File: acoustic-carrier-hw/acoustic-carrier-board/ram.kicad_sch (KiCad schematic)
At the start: 9 parts, among them IC1 ECP5-BGA256, U5 MT41K64M16TW-107_J-TR

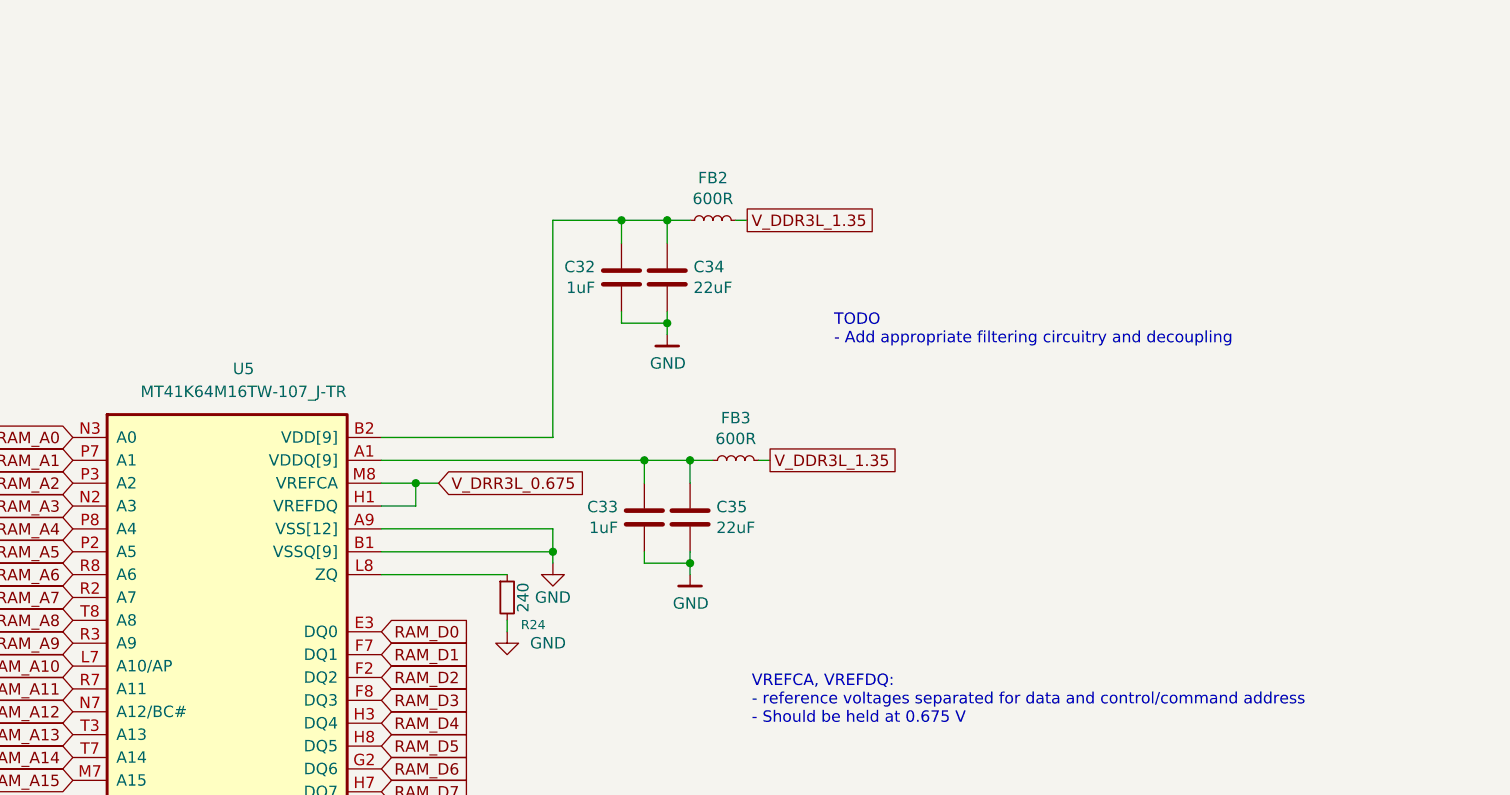
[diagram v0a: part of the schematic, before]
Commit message: [carrier] Added decoupling for DDR (next) Finish power supply
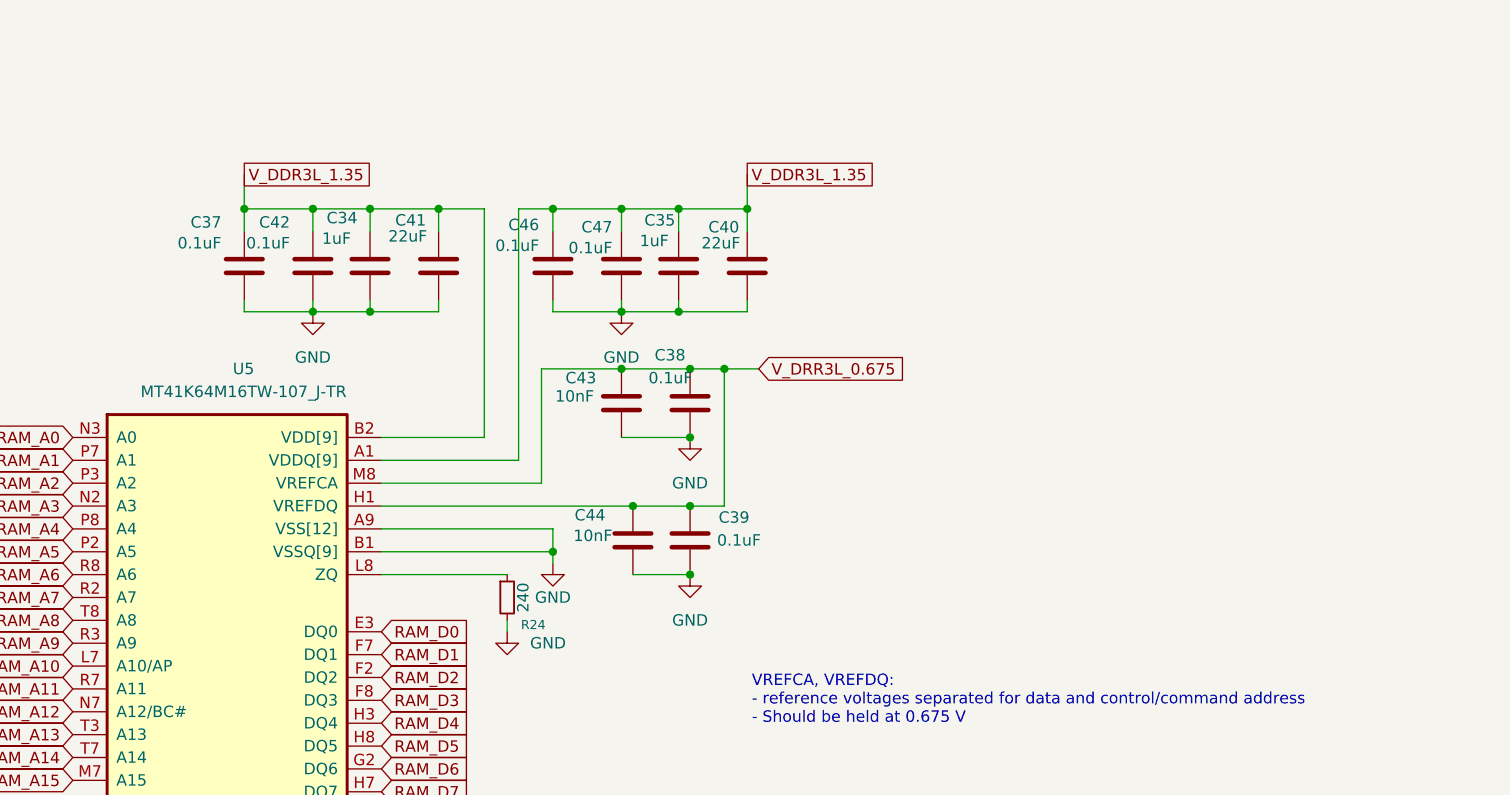
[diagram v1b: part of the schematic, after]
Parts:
- removed C32, C33: 1uF, Capacitor_SMD:C_0402_1005Metric, symbol Device:C
- removed FB2, FB3: 600R, Inductor_SMD:L_0402_1005Metric, symbol Device:L_Small
- added C37, C38, C39, C42, C46, C47: 0.1uF, Capacitor_SMD:C_0402_1005Metric, symbol Device:C
- added C40, C41: 22uF, Capacitor_SMD:C_0603_1608Metric, symbol Device:C
- added C43, C44: 10nF, Capacitor_SMD:C_0402_1005Metric, symbol Device:C
- C34, C35: value 22uF -> 1uF; footprint Capacitor_SMD:C_0603_1608Metric -> Capacitor_SMD:C_0805_2012Metric; LCSC Part Number (none) -> C28323; Manufacturing Part Number (none) -> CL21B105KBFNNNE; Mfg Murata Electronics North America -> (none); PN GRM188R60J226MEA0D -> (none)
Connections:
- net GND: now also C37.2, C38.2, C39.2, C40.2, C41.2, C42.2, C43.2, C44.2, C46.2, C47.2
- net V_DDR3L_1.35: now also C34.1, C35.1, U5.A1 (VDDQ[9]), U5.A8 (VDDQ), U5.B2 (VDD[9]), U5.C1 (VDDQ), U5.C9 (VDDQ), U5.D2 (VDDQ), U5.D9 (VDD), U5.E9 (VDDQ), U5.F1 (VDDQ), U5.G7 (VDD), U5.H2 (VDDQ), U5.H9 (VDDQ), U5.K2 (VDD), U5.K8 (VDD), U5.N1 (VDD), U5.N9 (VDD), U5.R1 (VDD), U5.R9 (VDD), C37.1, C40.1, C41.1, C42.1, C46.1, C47.1
- net V_DRR3L_0.675: now also C38.1, C39.1, C43.1, C44.1
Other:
- note removed: "TODO - Add appropriate filtering circuitry and decoupling"
- moved on the sheet: C34

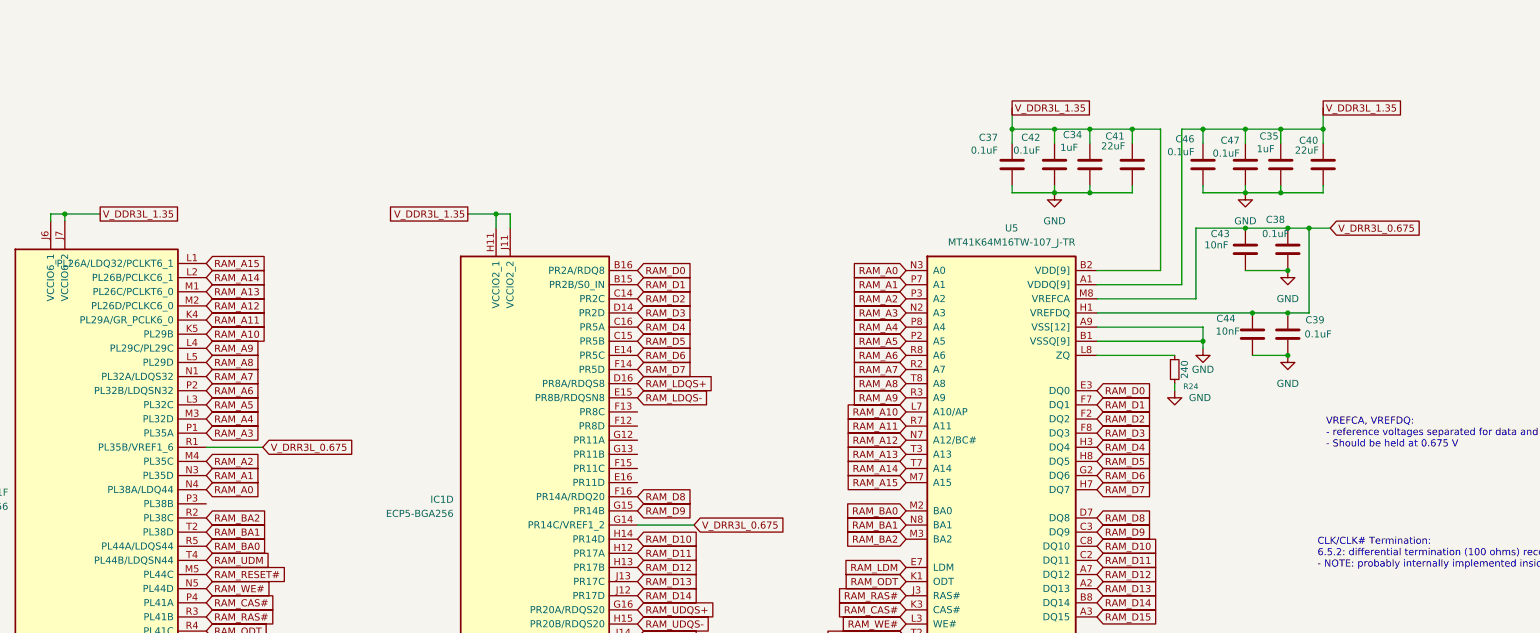
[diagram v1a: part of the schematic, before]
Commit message: added decoupling and power flags
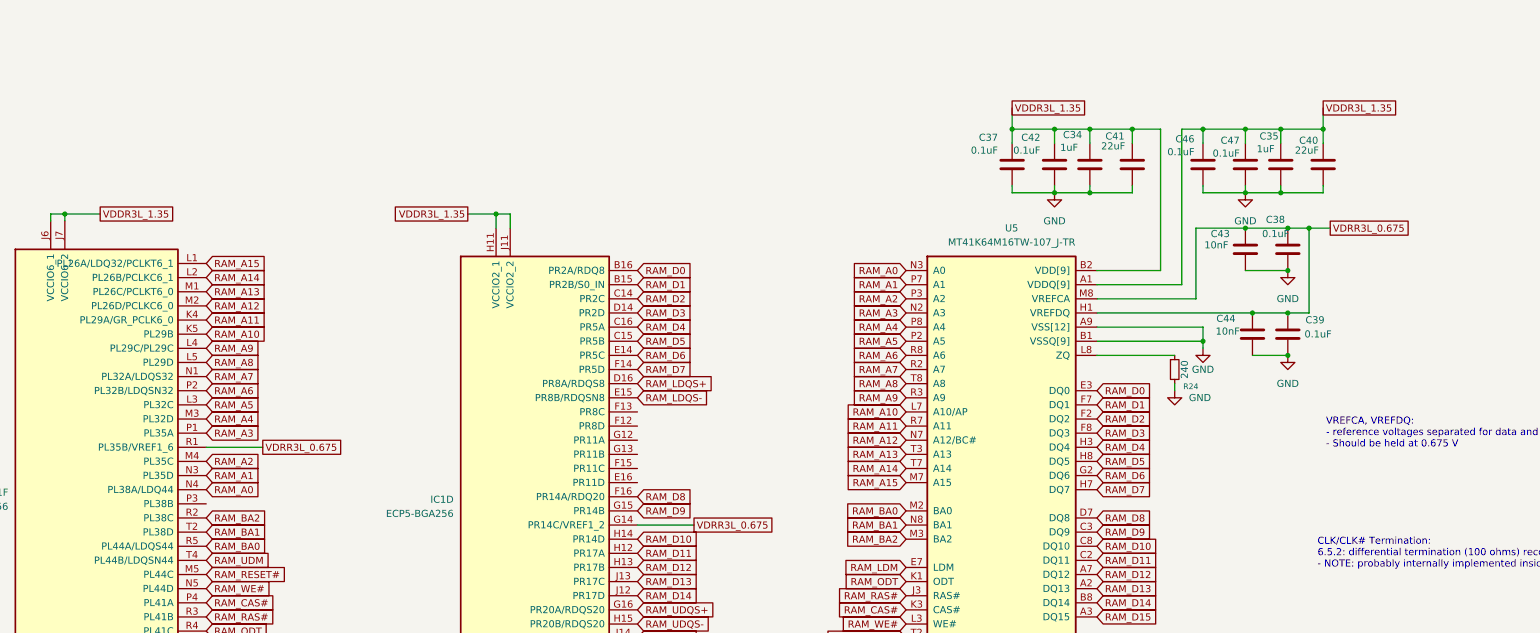
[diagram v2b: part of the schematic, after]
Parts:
- IC1: footprint BGA256C80P16X16_1400X1400X170 -> (none)
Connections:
- net V_DDR3L_1.35 renamed VDDR3L_1.35
- net V_DRR3L_0.675 renamed VDRR3L_0.675
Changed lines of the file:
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@@
 		)
 	)
-	(global_label "V_DRR3L_0.675"
-		(shape input)
-		(at 74.93 81.28 0)
-		(fields_autoplaced yes)
-		(effects
-			(font
-				(size 1.27 1.27)
-			)
-			(justify left)
-		)
-		(property "Intersheetrefs" "${INTERSHEET_REFS}"
-			(at 92.4294 81.28 0)
-			(effects
-				(font
-					(size 1.27 1.27)
-				)
-				(justify left)
-				(hide yes)
-			)
-		)
-	)
 	(global_label "RAM_A4"
 		(shape input)
@@
 		)
 	)
+	(global_label "VDDR3L_1.35"
+		(shape passive)
+		(at 111.76 39.37 180)
+		(fields_autoplaced yes)
+		(effects
+			(font
+				(size 1.27 1.27)
+			)
+			(justify right)
+		)
+		(property "Intersheetrefs" "${INTERSHEET_REFS}"
+			(at 97.549 39.37 0)
+			(effects
+				(font
+					(size 1.27 1.27)
+				)
+				(justify right)
+				(hide yes)
+			)
+		)
+	)
 	(global_label "RAM_CAS#"
 		(shape input)
@@
 		)
 	)
-	(global_label "V_DDR3L_1.35"
-		(shape passive)
-		(at 209.55 20.32 0)
-		(fields_autoplaced yes)
-		(effects
-			(font
-				(size 1.27 1.27)
-			)
-			(justify left)
-		)
-		(property "Intersheetrefs" "${INTERSHEET_REFS}"
-			(at 224.7286 20.32 0)
-			(effects
-				(font
-					(size 1.27 1.27)
-				)
-				(justify left)
-				(hide yes)
-			)
-		)
-	)
 	(global_label "RAM_RESET#"
 		(shape input)
@@
 		)
 	)
-	(global_label "V_DDR3L_1.35"
-		(shape passive)
-		(at 265.43 20.32 0)
-		(fields_autoplaced yes)
-		(effects
-			(font
-				(size 1.27 1.27)
-			)
-			(justify left)
-		)
-		(property "Intersheetrefs" "${INTERSHEET_REFS}"
-			(at 280.6086 20.32 0)
-			(effects
-				(font
-					(size 1.27 1.27)
-				)
-				(justify left)
-				(hide yes)
-			)
-		)
-	)
 	(global_label "RAM_CK-"
 		(shape input)
@@
 		)
 	)
+	(global_label "VDDR3L_1.35"
+		(shape passive)
+		(at 45.72 39.37 0)
+		(fields_autoplaced yes)
+		(effects
+			(font
+				(size 1.27 1.27)
+			)
+			(justify left)
+		)
+		(property "Intersheetrefs" "${INTERSHEET_REFS}"
+			(at 59.931 39.37 0)
+			(effects
+				(font
+					(size 1.27 1.27)
+				)
+				(justify left)
+				(hide yes)
+			)
+		)
+	)
 	(global_label "RAM_A1"
 		(shape input)
@@
 		)
 	)
+	(global_label "VDRR3L_0.675"
+		(shape passive)
+		(at 152.4 95.25 0)
+		(fields_autoplaced yes)
+		(effects
+			(font
+				(size 1.27 1.27)
+			)
+			(justify left)
+		)
+		(property "Intersheetrefs" "${INTERSHEET_REFS}"
+			(at 167.8205 95.25 0)
+			(effects
+				(font
+					(size 1.27 1.27)
+				)
+				(justify left)
+				(hide yes)
+			)
+		)
+	)
 	(global_label "RAM_A13"
 		(shape input)
@@
 		)
 	)
-	(global_label "RAM_D14"
-		(shape input)
-		(at 224.79 109.22 0)
+	(global_label "VDRR3L_0.675"
+		(shape passive)
+		(at 74.93 81.28 0)
+		(fields_autoplaced yes)
 		(effects
 			(font
@@
 		)
 		(property "Intersheetrefs" "${INTERSHEET_REFS}"
-			(at 224.79 109.22 0)
+			(at 90.3505 81.28 0)
 			(effects
 				(font
 					(size 1.27 1.27)
 				)
+				(justify left)
 				(hide yes)
 			)
 		)
 	)
-	(global_label "RAM_D10"
+	(global_label "RAM_D14"
 		(shape input)
-		(at 142.24 97.79 0)
+		(at 224.79 109.22 0)
 		(effects
 			(font
@@
 		)
 		(property "Intersheetrefs" "${INTERSHEET_REFS}"
-			(at 142.24 97.79 0)
+			(at 224.79 109.22 0)
 			(effects
 				(font
@@
 		)
 	)
-	(global_label "RAM_D11"
+	(global_label "RAM_D10"
 		(shape input)
-		(at 142.24 100.33 0)
+		(at 142.24 97.79 0)
 		(effects
 			(font
@@
 		)
 		(property "Intersheetrefs" "${INTERSHEET_REFS}"
-			(at 142.24 100.33 0)
+			(at 142.24 97.79 0)
 			(effects
 				(font
@@
 		)
 	)
-	(global_label "RAM_D8"
-		(shape input)
-		(at 142.24 90.17 0)
+	(global_label "VDDR3L_1.35"
+		(shape passive)
+		(at 265.43 20.32 0)
+		(fields_autoplaced yes)
 		(effects
 			(font
@@
 		)
 		(property "Intersheetrefs" "${INTERSHEET_REFS}"
-			(at 142.24 90.17 0)
+			(at 279.641 20.32 0)
 			(effects
 				(font
 					(size 1.27 1.27)
 				)
+				(justify left)
 				(hide yes)
 			)
 		)
 	)
-	(global_label "RAM_D15"
+	(global_label "RAM_D11"
 		(shape input)
-		(at 224.79 111.76 0)
+		(at 142.24 100.33 0)
 		(effects
 			(font
@@
 		)
 		(property "Intersheetrefs" "${INTERSHEET_REFS}"
-			(at 224.79 111.76 0)
+			(at 142.24 100.33 0)
 			(effects
 				(font
@@
 		)
 	)
-	(global_label "RAM_D9"
+	(global_label "RAM_D8"
 		(shape input)
-		(at 142.24 92.71 0)
+		(at 142.24 90.17 0)
 		(effects
 			(font
@@
 		)
 		(property "Intersheetrefs" "${INTERSHEET_REFS}"
-			(at 142.24 92.71 0)
+			(at 142.24 90.17 0)
 			(effects
 				(font
@@
 		)
 	)
-	(global_label "RAM_D11"
+	(global_label "RAM_D15"
 		(shape input)
-		(at 224.79 101.6 0)
+		(at 224.79 111.76 0)
 		(effects
 			(font
@@
 		)
 		(property "Intersheetrefs" "${INTERSHEET_REFS}"
-			(at 224.79 101.6 0)
+			(at 224.79 111.76 0)
 			(effects
 				(font
@@
 		)
 	)
-	(global_label "V_DRR3L_0.675"
+	(global_label "RAM_D9"
 		(shape input)
-		(at 152.4 95.25 0)
-		(fields_autoplaced yes)
+		(at 142.24 92.71 0)
 		(effects
 			(font
@@
 		)
 		(property "Intersheetrefs" "${INTERSHEET_REFS}"
-			(at 169.8994 95.25 0)
+			(at 142.24 92.71 0)
 			(effects
 				(font
 					(size 1.27 1.27)
 				)
-				(justify left)
 				(hide yes)
 			)
 		)
 	)
-	(global_label "RAM_LDM"
+	(global_label "RAM_D11"
 		(shape input)
-		(at 190.5 102.87 180)
+		(at 224.79 101.6 0)
 		(effects
 			(font
 				(size 1.27 1.27)
 			)
-			(justify right)
+			(justify left)
 		)
 		(property "Intersheetrefs" "${INTERSHEET_REFS}"
-			(at 190.5 102.87 0)
+			(at 224.79 101.6 0)
 			(effects
 				(font
@@
 		)
 	)
-	(global_label "V_DRR3L_0.675"
+	(global_label "RAM_LDM"
 		(shape input)
-		(at 266.7 41.91 0)
-		(fields_autoplaced yes)
+		(at 190.5 102.87 180)
 		(effects
 			(font
 				(size 1.27 1.27)
 			)
-			(justify left)
+			(justify right)
 		)
 		(property "Intersheetrefs" "${INTERSHEET_REFS}"
-			(at 284.1994 41.91 0)
+			(at 190.5 102.87 0)
 			(effects
 				(font
 					(size 1.27 1.27)
 				)
-				(justify left)
 				(hide yes)
 			)
@@
 		)
 	)
-	(global_label "V_DDR3L_1.35"
-		(shape passive)
-		(at 45.72 39.37 0)
-		(fields_autoplaced yes)
-		(effects
-			(font
-				(size 1.27 1.27)
-			)
-			(justify left)
-		)
-		(property "Intersheetrefs" "${INTERSHEET_REFS}"
-			(at 60.8986 39.37 0)
-			(effects
-				(font
-					(size 1.27 1.27)
-				)
-				(justify left)
-				(hide yes)
-			)
-		)
-	)
 	(global_label "RAM_A10"
 		(shape input)
@@
 		)
 	)
-	(global_label "V_DDR3L_1.35"
-		(shape passive)
-		(at 111.76 39.37 180)
-		(fields_autoplaced yes)
-		(effects
-			(font
-				(size 1.27 1.27)
-			)
-			(justify right)
-		)
-		(property "Intersheetrefs" "${INTERSHEET_REFS}"
-			(at 96.5814 39.37 0)
-			(effects
-				(font
-					(size 1.27 1.27)
-				)
-				(justify right)
-				(hide yes)
-			)
-		)
-	)
 	(global_label "RAM_D8"
 		(shape input)
@@
 		)
 	)
+	(global_label "VDDR3L_1.35"
+		(shape passive)
+		(at 209.55 20.32 0)
+		(fields_autoplaced yes)
+		(effects
+			(font
+				(size 1.27 1.27)
+			)
+			(justify left)
+		)
+		(property "Intersheetrefs" "${INTERSHEET_REFS}"
+			(at 223.761 20.32 0)
+			(effects
+				(font
+					(size 1.27 1.27)
+				)
+				(justify left)
+				(hide yes)
+			)
+		)
+	)
 	(global_label "RAM_BA2"
 		(shape input)
@@
 		)
 	)
+	(global_label "VDRR3L_0.675"
+		(shape passive)
+		(at 266.7 41.91 0)
+		(fields_autoplaced yes)
+		(effects
+			(font
+				(size 1.27 1.27)
+			)
+			(justify left)
+		)
+		(property "Intersheetrefs" "${INTERSHEET_REFS}"
+			(at 282.1205 41.91 0)
+			(effects
+				(font
+					(size 1.27 1.27)
+				)
+				(justify left)
+				(hide yes)
+			)
+		)
+	)
 	(global_label "RAM_A6"
 		(shape input)
@@
 			)
 		)
-		(property "Footprint" "BGA256C80P16X16_1400X1400X170"
+		(property "Footprint" ""
 			(at 46.99 1.27 0)
 			(effects
@@
 			)
 		)
-		(property "Footprint" "BGA256C80P16X16_1400X1400X170"
+		(property "Footprint" ""
 			(at -30.48 0 0)
 			(effects

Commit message: [carrier] Added decoupling to ethernet PHY
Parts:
- IC1: footprint (none) -> BGA256C80P16X16_1400X1400X170
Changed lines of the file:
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@@
 			)
 		)
-		(property "Footprint" ""
+		(property "Footprint" "BGA256C80P16X16_1400X1400X170"
 			(at 46.99 1.27 0)
 			(effects
@@
 			)
 		)
-		(property "Footprint" ""
+		(property "Footprint" "BGA256C80P16X16_1400X1400X170"
 			(at -30.48 0 0)
 			(effects

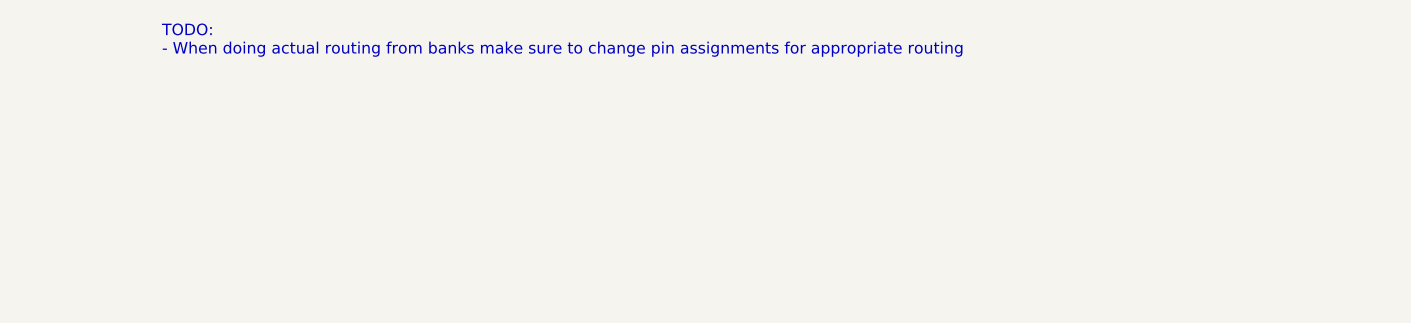
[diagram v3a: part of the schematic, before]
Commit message: [carrier] Finished basic ADC connections (next) decide on connections with power board
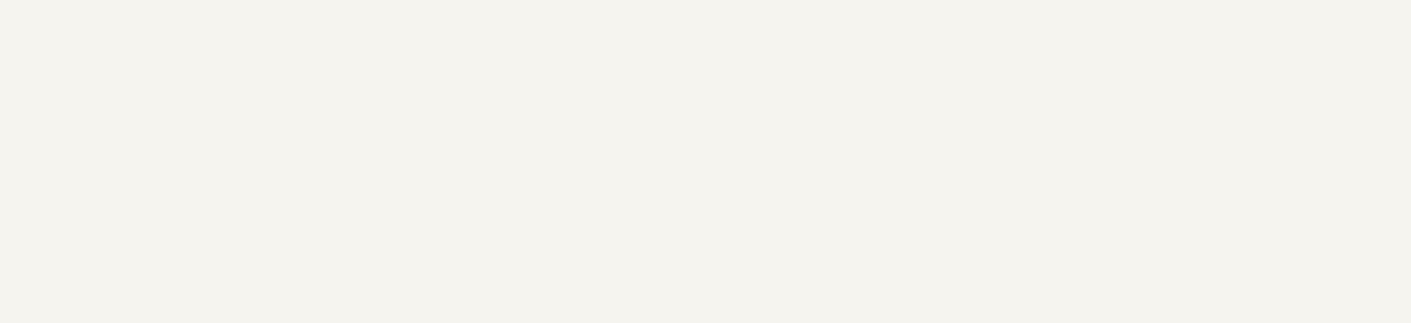
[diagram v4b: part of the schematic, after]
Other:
- note removed: "TODO: - When doing actual routing from banks make sure to change pin assignments for appropriate routing"
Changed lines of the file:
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@@
 	(generator_version "9.0")
 	(paper "A4")
-	(text "TODO: \n- When doing actual routing from banks make sure to change pin assignments for appropriate routing"
-		(exclude_from_sim no)
-		(at 21.082 -10.16 0)
-		(effects
-			(font
-				(size 1.27 1.27)
-			)
-			(justify left)
-		)
-	)
 	(text "Vref: \n- The DDR-logic requires an external 0.75 Volts (SSTL-15 standard).\n- External resistive divider required\nVcc: The DDRL-ram requires a 1.35 V supply voltage.\n- LDO / buck converter\nDQS-pins\n- Upper / Lower 8-bit synchronization for data\nData-pins:\n- upper 8 and lower 8 bits must belong to same DQS pins\nAddress / config pins\n- can be any DQ pins in the bank"
 		(exclude_from_sim no)

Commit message: [carrier] Reorganized carrier board schematic, added lcsc part numbers (next) check schematic before component placement
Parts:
- C34, C35: LCSC Part Number C28323 -> (none); LPN (none) -> C28323; MPN (none) -> CL21B105KBFNNNE; Manufacturing Part Number CL21B105KBFNNNE -> (none)
- C37, C38, C39, C42, C46, C47: LCSC Part Number C307331 -> (none); LPN (none) -> C307331; MPN (none) -> CL05B104KB54PNC; Manufacturing Part Number CL05B104KB54PNC -> (none)
- C40, C41: LCSC Part Number C59461 -> (none); LPN (none) -> C59461; MPN (none) -> CL10A226MQ8NRNC; Manufacturing Part Number CL10A226MQ8NRNC -> (none)
- C43, C44: LCSC Part Number C15195 -> (none); LPN (none) -> CL05B103KB5NNNC; MPN (none) -> C15195; Manufacturing Part Number CL05B103KB5NNNC -> (none)
- R24: LCSC Part Number C23350 -> (none); LPN (none) -> 0603WAF2400T5E; MPN (none) -> C23350; Manufacturing Part Number 0603WAF2400T5E -> (none)
- U5: LCSC Part Number C253882 -> (none); LPN (none) -> C253882; MPN (none) -> MT41K256M16TW-107:P; Manufacturing Part Number MT41K256M16TW-107:P -> (none)
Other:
- note added: "FPGA BANK DDR3L"
- note added: "RAM DDR3L"
